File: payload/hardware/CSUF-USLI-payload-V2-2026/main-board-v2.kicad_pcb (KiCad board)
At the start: 2 copper layers, 88.9 x 88.9 mm, 28 parts, among them J1 Servo JST, J10 8.4V IN, J11 Chassis Input, J12 Servo VCC, J13 Servo GND, J14 11.1V IN, J15 8.4V RESERVE, J16 11.1V RESERVE, J17 Driver Input, J2 Drill x 11.1V OUT, J4 BTS7960 Output, J6 Reserve JST, J9 Soil Sensor Power, Q3 IRLZ44N, U1 DEV-16771, U2 Adafruit BMP280, U3 RYLR896, U4 RYLR896, U5 Modbus to UART

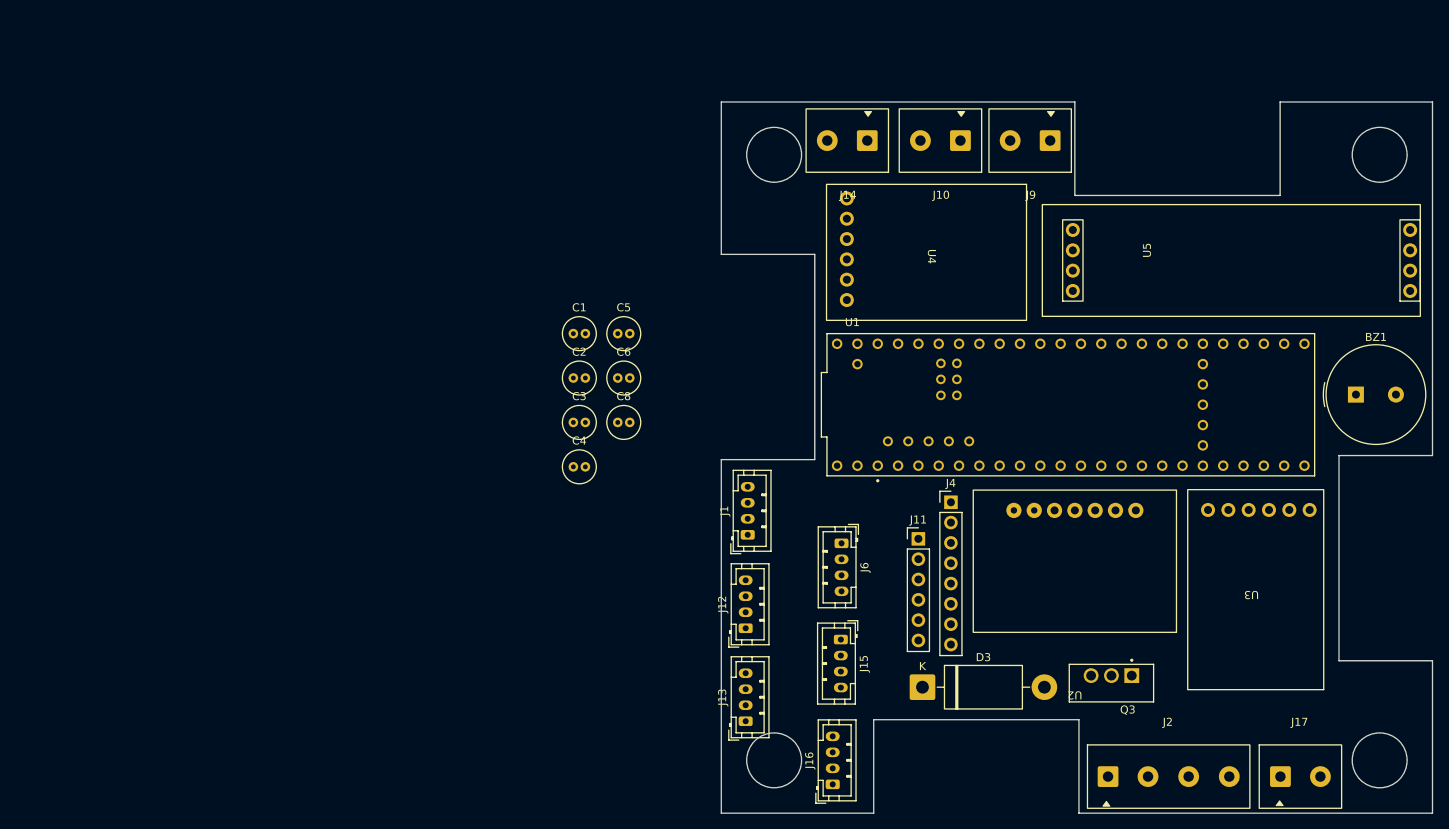
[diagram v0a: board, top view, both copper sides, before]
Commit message: Updated dimensions
Updated the position of the screw holes and slot. Made the corners rounded to match ig idk.
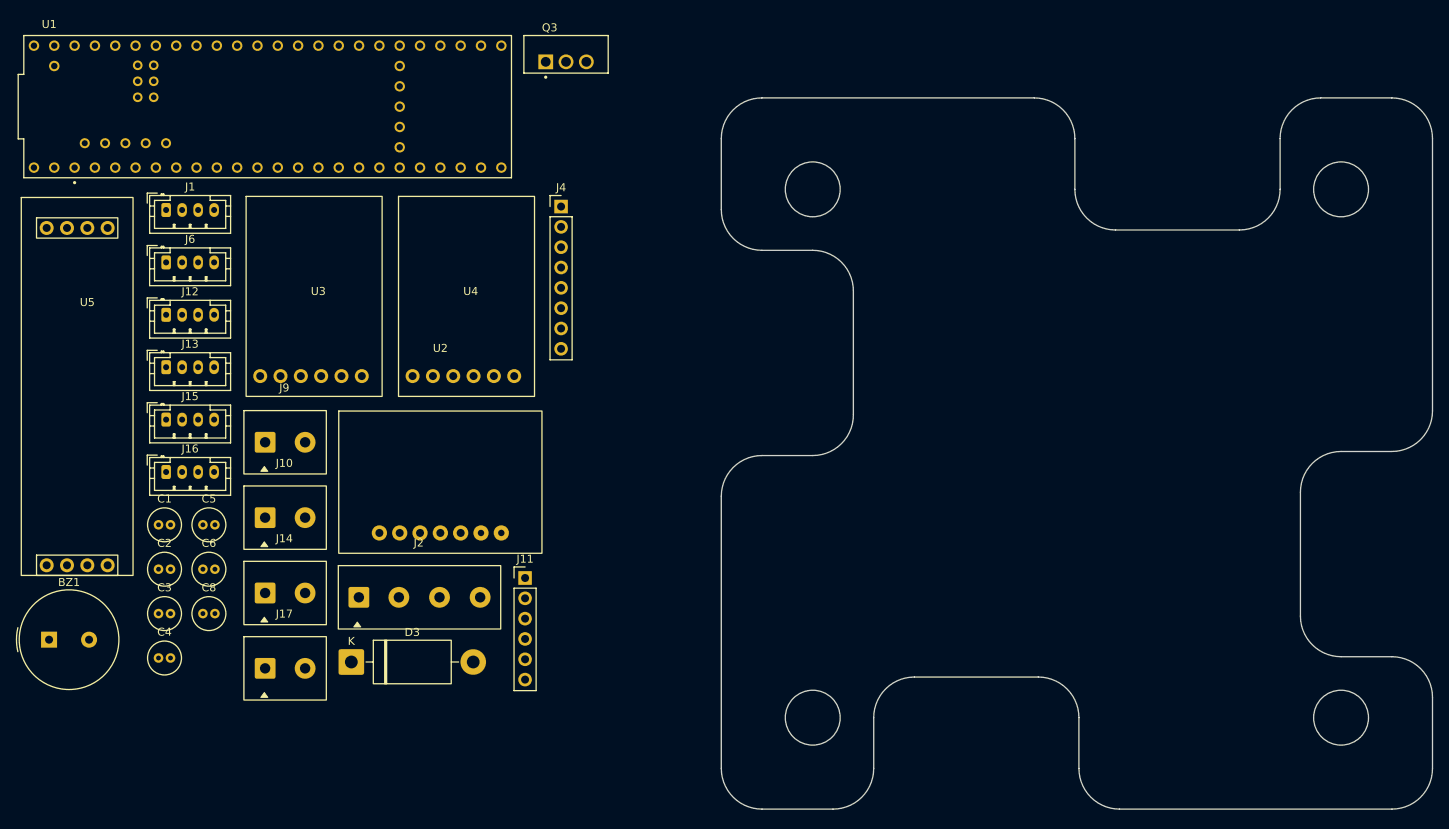
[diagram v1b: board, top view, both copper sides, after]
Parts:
- moved BZ1 166.2 mm to (43.0, 130.7)
- moved U3 137.2 mm to (68.2, 90.3), turned to 0 degrees
- moved U5 130.4 mm to (49.7, 88.1), turned to 0 degrees
- moved J17 127.6 mm to (72.5, 134.3)
- moved U1 107.1 mm to (70.3, 64.1)
- moved Q3 104.0 mm to (107.6, 57.5), turned to 0 degrees
- moved J9 100.5 mm to (72.5, 106.0), turned to 0 degrees
- moved J2 96.3 mm to (89.3, 125.4)
- moved J10 94.5 mm to (72.5, 115.5), turned to 0 degrees
- moved J16 92.0 mm to (57.6, 109.8), turned to 0 degrees
- moved J6 91.4 mm to (57.6, 83.6), turned to 0 degrees
- moved J14 90.2 mm to (72.5, 124.9), turned to 0 degrees
- moved J15 88.7 mm to (57.6, 103.2), turned to 0 degrees
- moved J13 84.9 mm to (57.6, 96.7), turned to 0 degrees
- moved J1 83.3 mm to (57.6, 77.0), turned to 0 degrees
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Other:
- outline, holes or cut-outs redrawn

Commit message: placing componenets
bruh
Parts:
- added C7: 330 uF, Capacitor_THT:C_Radial_D10.0mm_H12.5mm_P5.00mm, F.Cu at (135.9, 87.4)
- U2, U4, U5: moved to B.Cu
- moved J6 155.5 mm to (207.0, 126.7), turned to -90 degrees
- moved J15 127.8 mm to (185.3, 97.8)
- moved U5 126.3 mm to (165.1, 139.5), turned to -90 degrees
- moved U1 119.8 mm to (179.3, 113.8)
- moved C4 117.8 mm to (163.6, 83.6)
- moved U3 117.4 mm to (180.2, 125.4), turned to -90 degrees
- moved J17 116.4 mm to (171.5, 73.2), turned to 180 degrees
- moved J12 115.1 mm to (172.4, 97.8)
- moved J2 109.1 mm to (187.2, 77.2), turned to 180 degrees
- moved C1 106.0 mm to (158.9, 88.3)
- moved C5 105.2 mm to (163.6, 88.4)
- moved C6 104.1 mm to (158.9, 83.4)
- moved J16 102.6 mm to (159.5, 97.8)
- moved J14 102.1 mm to (160.5, 73.2), turned to 180 degrees
- moved BZ1 100.9 mm to (143.8, 134.9)
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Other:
- outline, holes or cut-outs redrawn

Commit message: trying to route traces
bad bad bad
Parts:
- moved C7 33.9 mm to (169.8, 86.3)
- moved Q3 33.1 mm to (203.3, 91.2)
- moved J13 26.7 mm to (173.4, 98.7)
- moved J16 26.6 mm to (186.2, 98.7)
- moved J15 24.7 mm to (160.6, 98.7)
- moved J12 24.6 mm to (147.8, 98.7)
- moved C1 22.0 mm to (159.6, 110.3)
- moved U2 13.3 mm to (184.5, 116.8)
- moved J6 0.60 mm to (207.3, 126.3), turned to 180 degrees
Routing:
- net +11.1V: track 0.00 -> 82.3 mm
- net Net-(BZ1-+): track 0.00 -> 81.9 mm
- net +8.4V: track 0.00 -> 57.5 mm
- net Chassis_Encoder_A: track 0.00 -> 43.4 mm
- net Chassis_Encoder_B: track 0.00 -> 41.3 mm, vias 0 -> 2
- net RX3: track 0.00 -> 33.0 mm, vias 0 -> 1
- net SERVO_3: track 0.00 -> 32.7 mm
- net Net-(D3-A): track 0.00 -> 30.6 mm
- net SERVO_2: track 0.00 -> 29.4 mm
- net SERVO_1: track 0.00 -> 26.1 mm
- net SERVO_0: track 0.00 -> 23.6 mm
- net RESERVE_0: track 0.00 -> 21.3 mm
- net SDA: track 0.00 -> 20.9 mm
- net SCL: track 0.00 -> 18.7 mm
- net +3V3: track 0.00 -> 14.6 mm
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
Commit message: pcb reroute
traces are doomed 0 errors on DRC!
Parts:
- removed D3: 1N5822, Diode_THT:D_DO-201AD_P15.24mm_Horizontal
- added J3: Motor Power, Phoenix_Screw_Connectors:Edit_TerminalBlock_Phoenix_MKDS-1,5-2_1x02_P5.00mm_Horizontal, F.Cu at (211.5, 85.0)
- moved Q3 64.5 mm to (139.1, 85.0), turned to 90 degrees
- moved C3 25.4 mm to (162.3, 91.5)
- moved J15 23.3 mm to (137.3, 98.7)
- moved J4 18.1 mm to (148.3, 126.8), turned to 90 degrees
- moved J16 15.7 mm to (201.8, 98.8)
- moved J11 12.2 mm to (181.8, 89.8), turned to 90 degrees
- moved J12 11.0 mm to (158.8, 98.7)
- moved J13 6.96 mm to (180.3, 98.8)
- moved C5 6.83 mm to (157.5, 91.5)
- moved BZ1 6.23 mm to (138.0, 132.5), turned to 90 degrees
- moved U3 6.16 mm to (176.4, 130.2)
- moved J10 5.10 mm to (149.6, 78.3)
- moved J14 5.10 mm to (160.5, 78.3)
- moved J17 5.10 mm to (171.5, 78.3)
- moved J9 5.10 mm to (149.6, 86.9)
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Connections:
- J11 pad 1: RPWM -> Net-(J11-Pin_1)
- J11 pad 2: LPWM -> Net-(J11-Pin_2)
- J11 pad 4: ENCODER_VCC -> +5V
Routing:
- net +3V3: track 14.6 -> 104.1 mm
- net +5V: track 12.9 -> 91.7 mm, vias 1 -> 4
- net DRILL: track 0.00 -> 70.2 mm, vias 0 -> 2
- net RX4: track 0.00 -> 44.8 mm
- net TX4: track 0.00 -> 38.9 mm
- net TX3: track 0.00 -> 37.6 mm
- net Net-(BZ1-+): track 81.9 -> 115.9 mm
- net Net-(J11-Pin_1): track 0.00 -> 32.7 mm
- net Net-(J11-Pin_2): track 0.00 -> 28.1 mm
- net TX6: track 0.00 -> 24.2 mm
- net SOIL_ENABLE: track 0.00 -> 19.5 mm
- net RX6: track 0.00 -> 18.7 mm, vias 0 -> 2
- net Chassis_Encoder_B: track 41.3 -> 58.0 mm, vias 2 -> 1
- net RESERVE_3: track 5.72 -> 22.0 mm, vias 1 -> 0
- net Net-(D3-A): track 30.6 -> 42.5 mm
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- added copper zone on B.Cu, net GND
- added copper zone on F.Cu, net GND
